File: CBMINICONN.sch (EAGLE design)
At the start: 8 parts

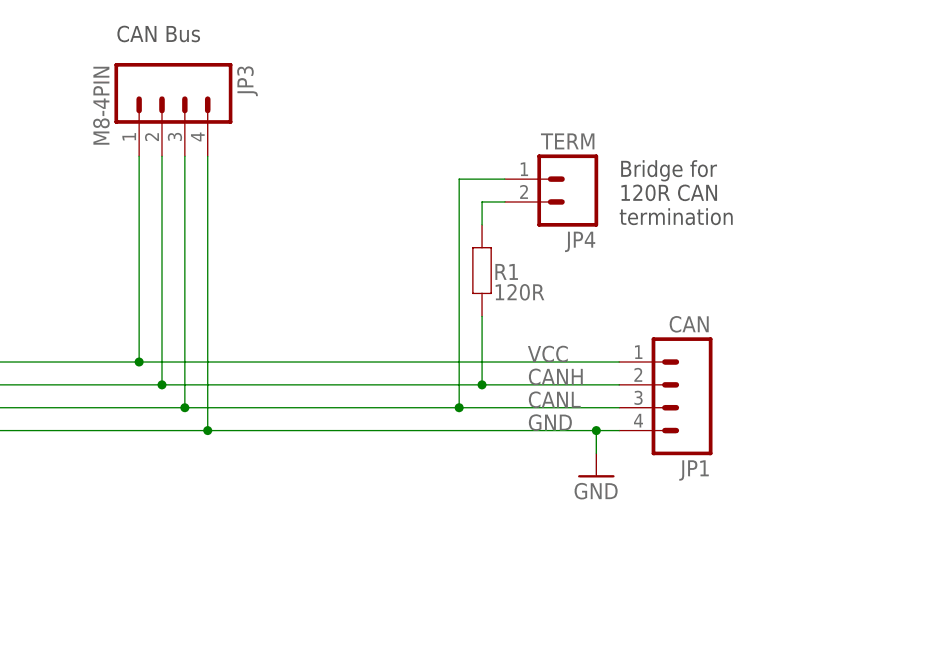
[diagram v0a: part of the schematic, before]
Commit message: Removed 120R termination, rotated connectors by 20 degrees, and added circular cut-out
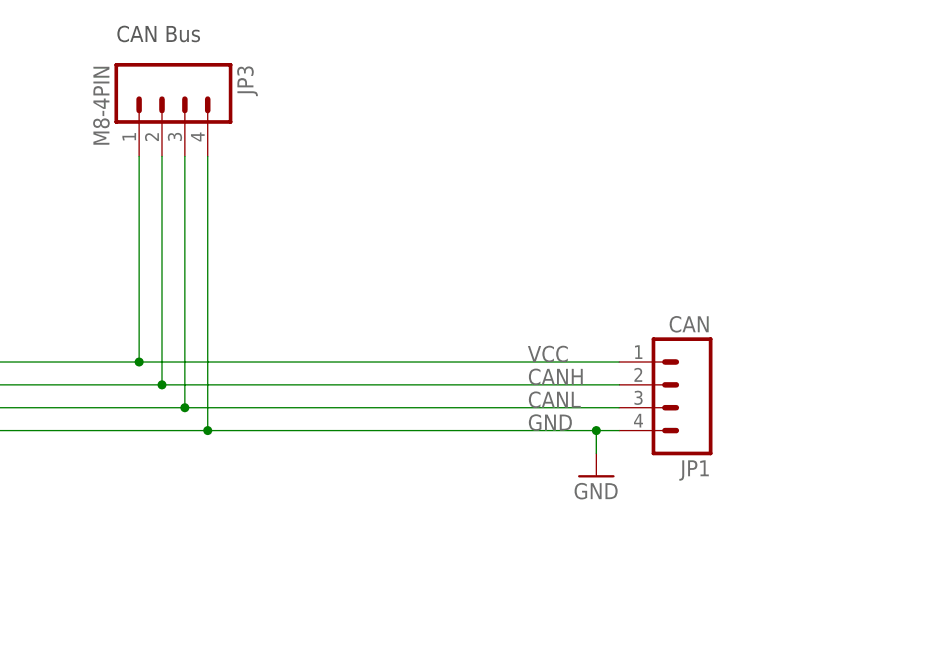
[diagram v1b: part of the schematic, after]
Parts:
- removed JP4: TERM, freetronics-jon:M02PTH
- removed R1: 120R, freetronics-master-v1.1:RESISTOR0603
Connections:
- removed net N$3: JP4.2, R1.2
- net CANH: no longer R1.1
- net CANL: no longer JP4.1
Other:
- note removed: "Bridge for 120R CAN termination"
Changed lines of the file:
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@@
 <?xml version="1.0" encoding="utf-8"?>
 <!DOCTYPE eagle SYSTEM "eagle.dtd">
-<eagle version="9.0.1">
+<eagle version="9.4.2">
 <drawing>
 <settings>
-<setting alwaysvectorfont="yes"/>
+<setting alwaysvectorfont="no"/>
 <setting keepoldvectorfont="yes"/>
 <setting verticaltext="up"/>
@@
 <part name="JP1" library="freetronics-jon" deviceset="M04" device="PTH" value="CAN"/>
 <part name="GND6" library="SparkFun" deviceset="GND" device=""/>
-<part name="JP4" library="freetronics-jon" deviceset="M02" device="PTH" value="TERM"/>
 <part name="LED1" library="freetronics-jon" deviceset="LED" device="3MM" value="GREEN"/>
 <part name="JP2" library="freetronics-jon" deviceset="M8-4PIN" device=""/>
 <part name="JP3" library="freetronics-jon" deviceset="M8-4PIN" device=""/>
-<part name="R1" library="freetronics-master-v1.1" deviceset="RESISTOR" device="0603" value="120R"/>
 </parts>
 <sheets>
@@
 <text x="86.36" y="137.16" size="1.778" layer="97">CAN Bus</text>
 <text x="116.84" y="137.16" size="1.778" layer="97">CAN Bus</text>
-<text x="172.72" y="116.84" size="1.778" layer="97">Bridge for
-120R CAN
-termination</text>
 </plain>
 <instances>
@@
 <attribute name="VALUE" x="59.69" y="110.998" size="1.778" layer="96"/>
 </instance>
-<instance part="JP1" gate="G$1" x="177.8" y="99.06" rot="R180"/>
-<instance part="GND6" gate="1" x="170.18" y="88.9"/>
-<instance part="JP4" gate="G$1" x="167.64" y="121.92" rot="R180"/>
-<instance part="LED1" gate="G$1" x="58.42" y="104.14"/>
-<instance part="JP2" gate="G$1" x="91.44" y="129.54" rot="R270"/>
-<instance part="JP3" gate="G$1" x="121.92" y="129.54" rot="R270"/>
-<instance part="R1" gate="G$1" x="157.48" y="111.76" smashed="yes" rot="R90">
-<attribute name="NAME" x="158.75" y="110.7186" size="1.778" layer="95"/>
-<attribute name="VALUE" x="158.75" y="108.458" size="1.778" layer="96"/>
+<instance part="JP1" gate="G$1" x="177.8" y="99.06" smashed="yes" rot="R180">
+<attribute name="VALUE" x="182.88" y="106.68" size="1.778" layer="96" rot="R180"/>
+<attribute name="NAME" x="182.88" y="90.678" size="1.778" layer="95" rot="R180"/>
+</instance>
+<instance part="GND6" gate="1" x="170.18" y="88.9" smashed="yes">
+<attribute name="VALUE" x="167.64" y="86.36" size="1.778" layer="96"/>
+</instance>
+<instance part="LED1" gate="G$1" x="58.42" y="104.14" smashed="yes">
+<attribute name="NAME" x="61.976" y="99.568" size="1.778" layer="95" rot="R90"/>
+<attribute name="VALUE" x="64.135" y="99.568" size="1.778" layer="96" rot="R90"/>
+</instance>
+<instance part="JP2" gate="G$1" x="91.44" y="129.54" smashed="yes" rot="R270">
+<attribute name="VALUE" x="83.82" y="134.62" size="1.778" layer="96" rot="R270"/>
+<attribute name="NAME" x="99.822" y="134.62" size="1.778" layer="95" rot="R270"/>
+</instance>
+<instance part="JP3" gate="G$1" x="121.92" y="129.54" smashed="yes" rot="R270">
+<attribute name="VALUE" x="114.3" y="134.62" size="1.778" layer="96" rot="R270"/>
+<attribute name="NAME" x="130.302" y="134.62" size="1.778" layer="95" rot="R270"/>
 </instance>
 </instances>
@@
 <label x="162.56" y="99.06" size="1.778" layer="95"/>
 <pinref part="JP1" gate="G$1" pin="2"/>
-<wire x1="172.72" y1="99.06" x2="157.48" y2="99.06" width="0.1524" layer="91"/>
-<pinref part="R1" gate="G$1" pin="1"/>
-<wire x1="157.48" y1="99.06" x2="121.92" y2="99.06" width="0.1524" layer="91"/>
+<wire x1="172.72" y1="99.06" x2="121.92" y2="99.06" width="0.1524" layer="91"/>
 <wire x1="121.92" y1="99.06" x2="91.44" y2="99.06" width="0.1524" layer="91"/>
-<wire x1="157.48" y1="106.68" x2="157.48" y2="99.06" width="0.1524" layer="91"/>
-<junction x="157.48" y="99.06"/>
 <pinref part="JP3" gate="G$1" pin="2"/>
 <wire x1="121.92" y1="124.46" x2="121.92" y2="99.06" width="0.1524" layer="91"/>
@@
 <label x="162.56" y="96.52" size="1.778" layer="95"/>
 <pinref part="JP1" gate="G$1" pin="3"/>
-<wire x1="172.72" y1="96.52" x2="154.94" y2="96.52" width="0.1524" layer="91"/>
-<pinref part="JP4" gate="G$1" pin="1"/>
-<wire x1="154.94" y1="96.52" x2="124.46" y2="96.52" width="0.1524" layer="91"/>
+<wire x1="172.72" y1="96.52" x2="124.46" y2="96.52" width="0.1524" layer="91"/>
 <wire x1="124.46" y1="96.52" x2="93.98" y2="96.52" width="0.1524" layer="91"/>
-<wire x1="160.02" y1="121.92" x2="154.94" y2="121.92" width="0.1524" layer="91"/>
-<wire x1="154.94" y1="121.92" x2="154.94" y2="96.52" width="0.1524" layer="91"/>
-<junction x="154.94" y="96.52"/>
 <pinref part="JP3" gate="G$1" pin="3"/>
 <wire x1="124.46" y1="124.46" x2="124.46" y2="96.52" width="0.1524" layer="91"/>
@@
 </segment>
 </net>
-<net name="N$3" class="0">
-<segment>
-<pinref part="JP4" gate="G$1" pin="2"/>
-<wire x1="160.02" y1="119.38" x2="157.48" y2="119.38" width="0.1524" layer="91"/>
-<pinref part="R1" gate="G$1" pin="2"/>
-<wire x1="157.48" y1="119.38" x2="157.48" y2="116.84" width="0.1524" layer="91"/>
-</segment>
-</net>
